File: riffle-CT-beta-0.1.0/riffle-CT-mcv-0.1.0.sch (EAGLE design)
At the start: 31 parts, among them IC1 MCP3221, IC5 TPS60400DBV

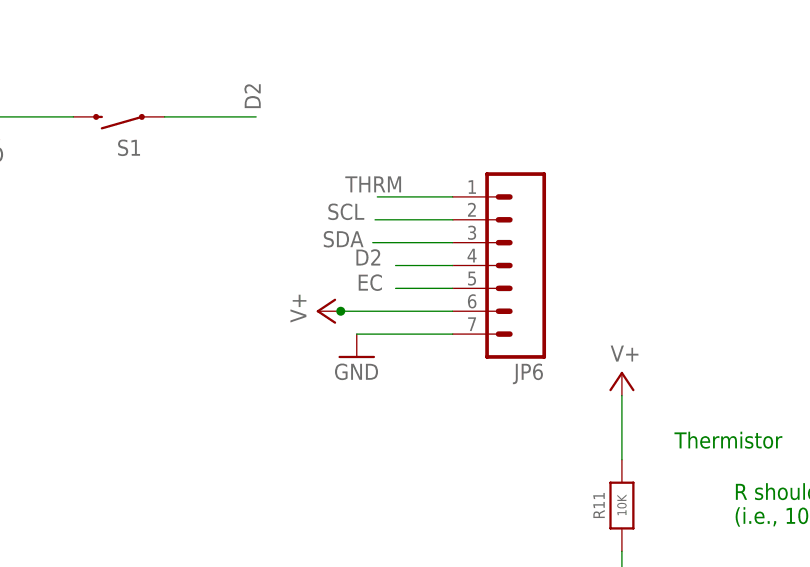
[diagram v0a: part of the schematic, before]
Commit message: optimized layout of parts
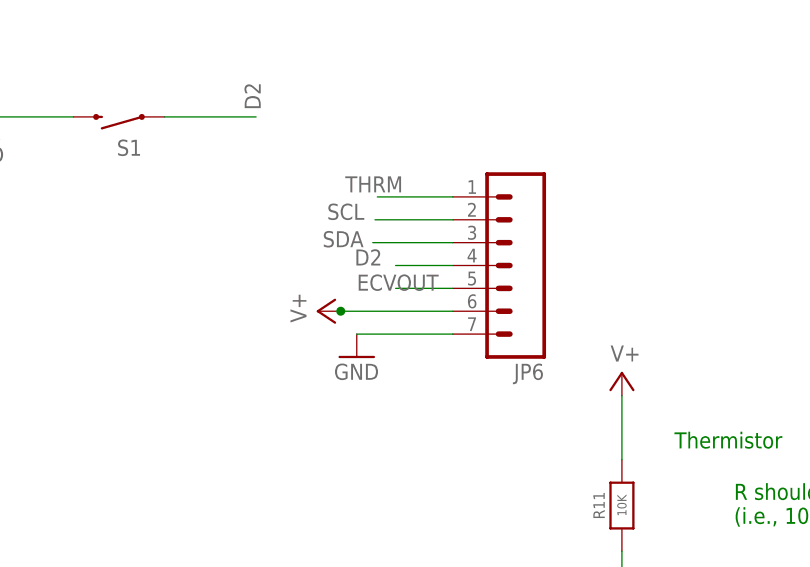
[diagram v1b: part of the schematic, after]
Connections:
- removed net EC: JP6.5
- net ECVOUT: now also JP6.5
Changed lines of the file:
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@@
 <setting verticaltext="up"/>
 </settings>
-<grid distance="0.01" unitdist="inch" unit="inch" style="lines" multiple="1" display="no" altdistance="0.01" altunitdist="inch" altunit="inch"/>
+<grid distance="0.1" unitdist="inch" unit="inch" style="lines" multiple="1" display="no" altdistance="0.01" altunitdist="inch" altunit="inch"/>
 <layers>
 <layer number="1" name="Top" color="4" fill="1" visible="no" active="no"/>
@@
 <label x="142.24" y="45.72" size="1.778" layer="95" xref="yes"/>
 </segment>
+<segment>
+<pinref part="JP6" gate="G$1" pin="5"/>
+<wire x1="80.518" y1="146.304" x2="74.168" y2="146.304" width="0.1524" layer="91"/>
+<label x="69.85" y="146.05" size="1.778" layer="95"/>
+</segment>
 </net>
 <net name="N$30" class="0">
@@
 </segment>
 </net>
-<net name="EC" class="0">
-<segment>
-<pinref part="JP6" gate="G$1" pin="5"/>
-<wire x1="80.518" y1="146.304" x2="74.168" y2="146.304" width="0.1524" layer="91"/>
-<label x="69.85" y="146.05" size="1.778" layer="95"/>
-</segment>
-</net>
